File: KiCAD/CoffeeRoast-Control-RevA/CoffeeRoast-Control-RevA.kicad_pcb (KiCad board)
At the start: 2 copper layers, 160 x 100 mm, 68 parts, among them J1 24V_IN_FROM_230V_PSU_3A, J2 FAN_24V_PWM_3A, J3 SSR_INPUT_TO_EXTERNAL_SSR, J4 K_TYPE_THERMOCOUPLE, J5 USB_C_Receptacle_XKB_U262-16X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, Q1 IRLZ44N_OR_LOGIC_NMOS, Q2 2N7002_SSR_DRIVER, SW1 RESET_EN, SW2 BOOT, U1 ESP32-S3-WROOM-1, U2 MAX6675_SOIC8_3V3, U3 AMS1117-3.3, U4 24V_TO_5V_BUCK_MODULE_>=1A

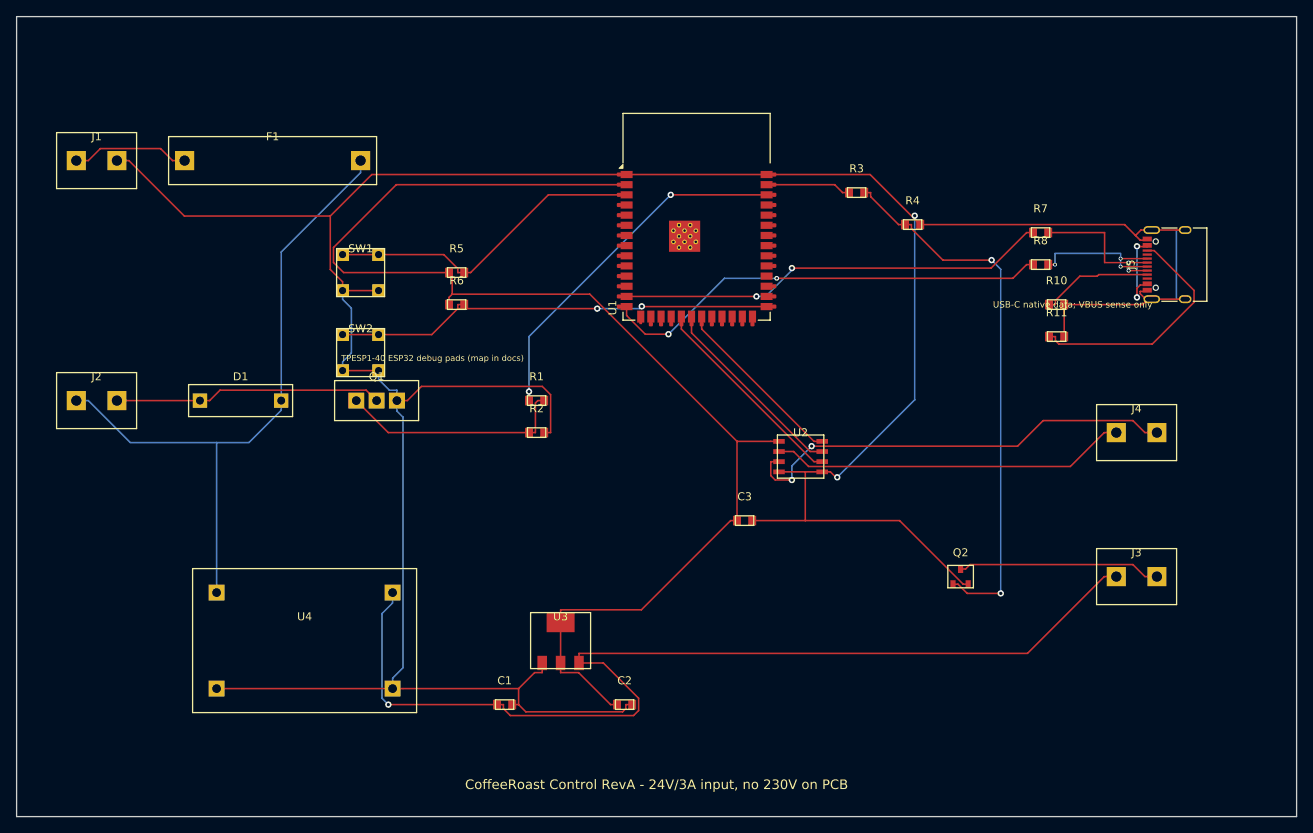
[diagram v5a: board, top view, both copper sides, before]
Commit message: Route labeled ESP32 solder pads outward
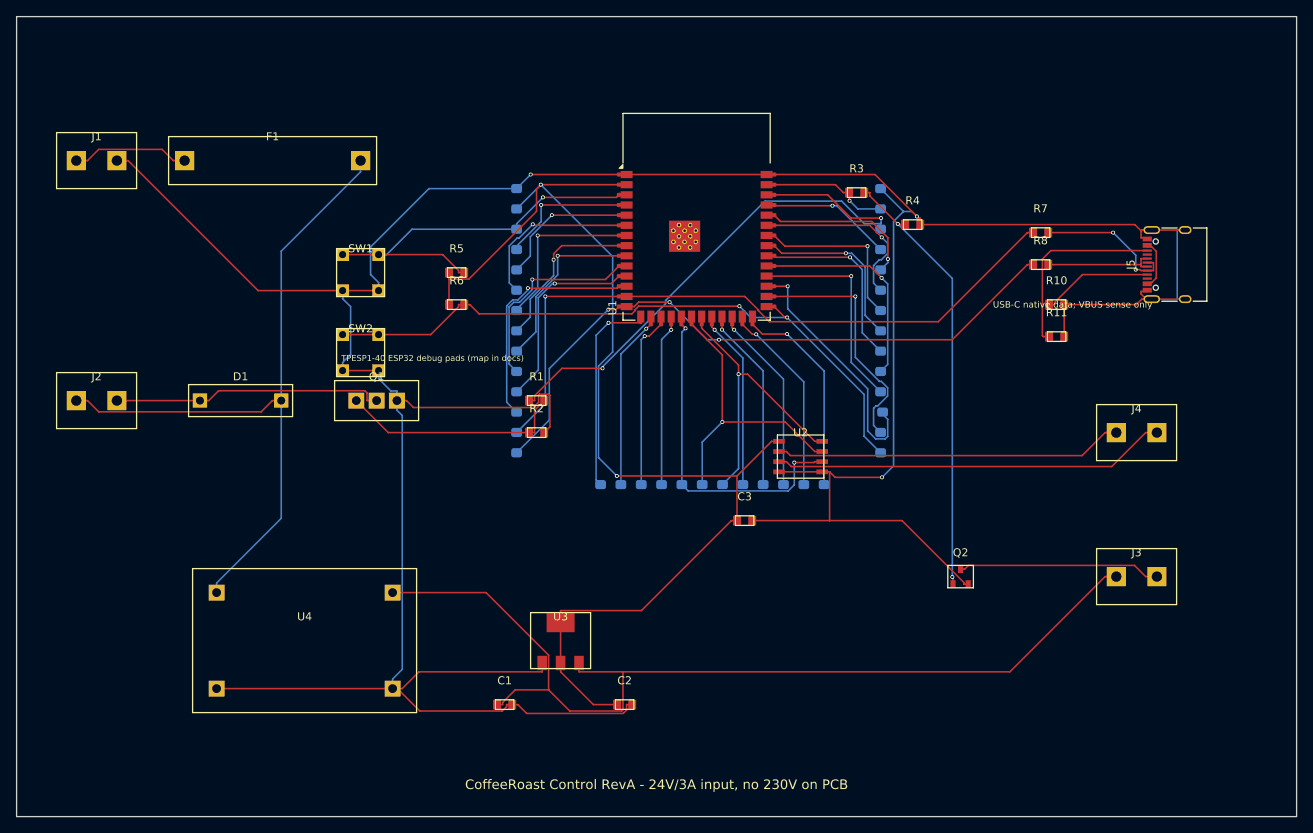
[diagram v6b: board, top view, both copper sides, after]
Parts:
- added PADESP1: GND, , B.Cu at (62.5, 21.5)
- added PADESP10: IO17, , B.Cu at (62.5, 44.4)
- added PADESP11: IO18, , B.Cu at (62.5, 46.9)
- added PADESP12: IO8, , B.Cu at (62.5, 49.4)
- added PADESP13: USB_D-, , B.Cu at (62.5, 52.0)
- added PADESP14: USB_D+, , B.Cu at (62.5, 54.5)
- added PADESP15: IO3, , B.Cu at (73.0, 58.5)
- added PADESP16: IO46, , B.Cu at (75.5, 58.5)
- added PADESP17: IO9, , B.Cu at (78.1, 58.5)
- added PADESP18: IO10, , B.Cu at (80.6, 58.5)
- added PADESP19: IO11, , B.Cu at (83.2, 58.5)
- added PADESP2: 3V3, , B.Cu at (62.5, 24.0)
- added PADESP20: IO12, , B.Cu at (85.7, 58.5)
- added PADESP21: IO13, , B.Cu at (88.2, 58.5)
- added PADESP22: IO14, , B.Cu at (90.8, 58.5)
- added PADESP23: IO21, , B.Cu at (93.3, 58.5)
- added PADESP24: IO47, , B.Cu at (95.9, 58.5)
- added PADESP25: IO48, , B.Cu at (98.4, 58.5)
- added PADESP26: IO45, , B.Cu at (100.9, 58.5)
- added PADESP27: IO0, , B.Cu at (108.0, 54.5)
- added PADESP28: IO35, , B.Cu at (108.0, 52.0)
- added PADESP29: IO36, , B.Cu at (108.2, 49.4)
- added PADESP3: EN, , B.Cu at (62.5, 26.6)
- added PADESP30: IO37, , B.Cu at (108.0, 46.9)
- added PADESP31: IO38, , B.Cu at (108.0, 44.4)
- added PADESP32: IO39, , B.Cu at (108.0, 41.8)
- added PADESP33: IO40, , B.Cu at (108.0, 39.3)
- added PADESP34: IO41, , B.Cu at (108.0, 36.7)
- added PADESP35: IO42, , B.Cu at (108.0, 34.2)
- added PADESP36: RXD0, , B.Cu at (108.0, 31.7)
- added PADESP37: TXD0, , B.Cu at (108.0, 29.1)
- added PADESP38: IO2, , B.Cu at (108.0, 26.6)
- added PADESP39: IO1, , B.Cu at (108.0, 24.0)
- added PADESP4: IO4, , B.Cu at (62.5, 29.1)
- added PADESP40: GND, , B.Cu at (108.0, 21.5)
- added PADESP5: IO5, , B.Cu at (62.5, 31.7)
- added PADESP6: IO6, , B.Cu at (62.5, 34.2)
- added PADESP7: IO7, , B.Cu at (62.5, 36.7)
- added PADESP8: IO15, , B.Cu at (62.5, 39.3)
- added PADESP9: IO16, , B.Cu at (62.5, 41.8)
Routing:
- net GPIO36: track 0.00 -> 31.3 mm, vias 0 -> 1
- net USB_DN_MCU: track 54.3 -> 85.4 mm, vias 2 -> 1
- net GPIO35: track 0.00 -> 31.1 mm, vias 0 -> 1
- net GPIO8: track 0.00 -> 29.9 mm, vias 0 -> 1
- net FAN_PWM: track 45.0 -> 73.1 mm
- net BOOT: track 55.8 -> 83.7 mm
- net GPIO38: track 0.00 -> 27.4 mm, vias 0 -> 1
- net GPIO37: track 0.00 -> 26.6 mm, vias 0 -> 1
- net GPIO45: track 0.00 -> 26.5 mm, vias 0 -> 1
- net GPIO17: track 0.00 -> 26.0 mm, vias 0 -> 1
- net GPIO3: track 0.00 -> 25.9 mm, vias 0 -> 1
- net USB_DP_MCU: track 56.5 -> 82.0 mm, vias 2 -> 3
- net GPIO18: track 0.00 -> 25.0 mm, vias 0 -> 1
- net GPIO48: track 0.00 -> 24.5 mm, vias 0 -> 1
- net GPIO39: track 0.00 -> 23.8 mm, vias 0 -> 1
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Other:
- board text added: "3V3"
- board text added: "EN"
- board text added: "ESP32 SOLDER PADS - BOTTOM"
- board text added: "GND"
- board text added: "IO0"
- board text added: "IO1"
- board text added: "IO10"
- board text added: "IO11"
- board text added: "IO12"
- board text added: "IO13"
- board text added: "IO14"
- board text added: "IO15"
- board text added: "IO16"
- board text added: "IO17"
- board text added: "IO18"
- board text added: "IO2"
- board text added: "IO21"
- board text added: "IO3"
- board text added: "IO35"
- board text added: "IO36"
- board text added: "IO37"
- board text added: "IO38"
- board text added: "IO39"
- board text added: "IO4"
- board text added: "IO40"
- board text added: "IO41"
- board text added: "IO42"
- board text added: "IO45"
- board text added: "IO46"
- board text added: "IO47"
- board text added: "IO48"
- board text added: "IO5"
- board text added: "IO6"
- board text added: "IO7"
- board text added: "IO8"
- board text added: "IO9"
- board text added: "RXD0"
- board text added: "TXD0"
- board text added: "USB_D+"
- board text added: "USB_D-"

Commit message: Improve CoffeeRoast RevA PCB robustness
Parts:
- added C4: 220uF_35V_INPUT_BULK, , F.Cu at (0.00, 0.00)
- added C5: 1nF_C0G_THERMO_DIFF_FILTER_DNP_IF_NOISY, , F.Cu at (0.00, 0.00)
- added D2: SMBJ33A_24V_INPUT_TVS, , F.Cu at (0.00, 0.00)
- added D3: SMBJ33A_FAN_TVS, , F.Cu at (0.00, 0.00)
- added TP24V: +24V_FUSED_TEST, , F.Cu at (0.00, 0.00)
- added TP3V3: +3V3_TEST, , F.Cu at (0.00, 0.00)
- added TP5V: +5V_TEST, , F.Cu at (0.00, 0.00)
- added TPGND: GND_TEST, , F.Cu at (0.00, 0.00)
- added U5: USBLC6-2SC6_OR_USB2_ESD, , F.Cu at (0.00, 0.00)
- Q1: value IRLZ44N_OR_LOGIC_NMOS -> IRLB8721_OR_3V3_LOGIC_NMOS_RDS_ON_LOW
- U3: value AMS1117-3.3 -> 3V3_SWITCHING_REGULATOR_>=600mA_5V_IN_REPLACES_AMS1117
- U4: value 24V_TO_5V_BUCK_MODULE_>=1A -> 24V_TO_5V_BUCK_MODULE_>=1A_LOW_NOISE
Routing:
- net GND: track 436.6 -> 447.8 mm
- net +24V_RAW: track 14.7 -> 22.9 mm
- net +24V_FUSED: track 88.2 -> 96.2 mm
- net THERMO_PLUS: track 43.6 -> 48.6 mm
- net THERMO_MINUS: track 49.3 -> 54.3 mm
- net FAN_NEG: track 34.1 -> 39.1 mm
- net +3V3: track 149.6 -> 153.6 mm
- net +5V: track 122.8 -> 125.8 mm

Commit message: feat: update RevA PCB and production artifacts
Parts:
- added C6: 100nF_U1_DECOUPLING_0603, , F.Cu at (73.2, 20.4)
- added C7: 100nF_U4_OUTPUT_DECOUPLING_0603, , F.Cu at (53.0, 72.7)
- added FID1: FIDUCIAL_GLOBAL_1MM, , F.Cu at (6.00, 6.00)
- added FID2: FIDUCIAL_GLOBAL_1MM, , F.Cu at (154.0, 6.00)
- added FID3: FIDUCIAL_GLOBAL_1MM, , F.Cu at (154.0, 94.0)
- added FID4: FIDUCIAL_GLOBAL_1MM, , B.Cu at (6.00, 6.00)
- added FID5: FIDUCIAL_GLOBAL_1MM, , B.Cu at (154.0, 6.00)
- added FID6: FIDUCIAL_GLOBAL_1MM, , B.Cu at (154.0, 94.0)
- added JGPIO1: ESP32_GPIO_BREAKOUT_ROW, ESP32_GPIO_BREAKOUT_ROW, F.Cu at (110.3, 92.0)
- added TPBOOT1: BOOT_TWEEZER_PADS, , F.Cu at (49.0, 42.0)
- added TPRESET1: RESET_TWEEZER_PADS, , F.Cu at (49.0, 32.0)
- added TPSSR1: SSR_OUT_MEAS_PADS, , F.Cu at (140.0, 76.2)
- moved C5 147.7 mm to (140.0, 47.0)
- moved U5 136.6 mm to (133.7, 28.0)
- moved TP3V3 104.7 mm to (72.0, 76.0)
- moved TPGND 97.8 mm to (50.0, 84.0)
- moved TP5V 87.7 mm to (50.0, 72.0)
- moved TP24V 75.3 mm to (22.0, 72.0)
- moved D3 44.1 mm to (10.0, 43.0)
- moved D2 28.0 mm to (10.0, 26.2)
- moved C4 25.3 mm to (10.0, 23.2)
- moved J5 9.00 mm to (154.0, 31.0)
- moved U1 3.00 mm to (85.0, 28.0)
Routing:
- net GPIO3: track 25.9 -> 71.5 mm
- net GPIO9: track 22.3 -> 68.0 mm
- net GPIO46: track 22.6 -> 68.2 mm
- net GPIO10: track 21.5 -> 67.1 mm
- net GPIO48: track 24.5 -> 61.5 mm
- net GPIO45: track 26.5 -> 63.5 mm
- net GND: track 447.8 -> 476.0 mm, vias 3 -> 5
- net +3V3: track 153.6 -> 171.7 mm, vias 2 -> 9
- net +5V: track 125.8 -> 138.0 mm
- net SSR_NEG: track 25.3 -> 37.3 mm
- net USB_DP: track 14.2 -> 23.2 mm
- net USB_CC2: track 24.0 -> 33.0 mm
- net USB_DN: track 18.0 -> 27.0 mm
- net USB_CC1: track 14.0 -> 23.0 mm
- net +24V_FUSED: track 96.2 -> 101.7 mm
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- added copper zone on B.Cu, net GND
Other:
- board text added: "+24V"
- board text added: "+5V"
- board text added: "+5V TP"
- board text added: "24V IN"
- board text added: "BOOT"
- board text added: "BOOT TP"
- board text added: "C1 10u"
- board text added: "C2 10u"
- board text added: "C3 100n"
- board text added: "C4 220uF"
- board text added: "C5 TC FILTER"
- board text added: "C6 100n U1"
- board text added: "C7 100n U4"
- board text added: "D1 FLYBACK"
- board text added: "D2 24V TVS"
- board text added: "D3 FAN TVS"
- board text added: "ESP32 GPIO BREAKOUT"
- board text added: "F1 FUSE"
- board text added: "FAN OUT"
- board text added: "FAN-"
- board text added: "GPIO0 BOOT"
- board text added: "GPIO1 SSR"
- board text added: "GPIO10"
- board text added: "GPIO11 DO"
- board text added: "GPIO12 CS"
- board text added: "GPIO13 CLK"
- board text added: "GPIO14"
- board text added: "GPIO15"
- board text added: "GPIO16"
- board text added: "GPIO17"
- board text added: "GPIO18"
- board text added: "GPIO19 D-"
- board text added: "GPIO2 FAN"
- board text added: "GPIO20 D+"
- board text added: "GPIO21"
- board text added: "GPIO3"
- board text added: "GPIO35"
- board text added: "GPIO36"
- board text added: "GPIO37"
- board text added: "GPIO38"
- board text added: "GPIO39"
- board text added: "GPIO4"
- board text added: "GPIO40"
- board text added: "GPIO41"
- board text added: "GPIO42"
- board text added: "GPIO45"
- board text added: "GPIO46"
- board text added: "GPIO47"
- board text added: "GPIO48"
- board text added: "GPIO5"
- board text added: "GPIO6"
- board text added: "GPIO7"
- board text added: "GPIO8"
- board text added: "GPIO9"
- board text added: "Q1 FAN MOSFET"
- board text added: "Q2 SSR DRV"
- board text added: "R1 100R"
- board text added: "R10 5k1"
- board text added: "R11 5k1"
- board text added: "R2 100k"
- board text added: "R3 100R"
- board text added: "R4 100k"
- board text added: "R5 10k"
- board text added: "R6 10k"
- board text added: "R7 27R"
- board text added: "R8 27R"
- board text added: "RESET"
- board text added: "RST"
- board text added: "RST TP"
- board text added: "RX0 GPIO44"
- board text added: "SSR MEAS"
- board text added: "SSR OUT"
- board text added: "SSR-"
- board text added: "SSR- TP"
- board text added: "TC+"
- board text added: "TC-"
- board text added: "THERMO"
- board text added: "TP24V"
- board text added: "TP3V3"
- board text added: "TP5V"
- board text added: "TPGND"
- board text added: "TX0 GPIO43"
- board text added: "U1 ESP32-S3"
- board text added: "U2 MAX6675"
- board text added: "U3 3V3 REG"
- board text added: "U4 24V->5V"
- board text added: "U5 USB ESD"
- board text added: "USB-C DATA"
- board text removed: "ESP32 SOLDER PADS - BOTTOM"
- board text removed: "IO0"
- board text removed: "IO1"
- board text removed: "IO10"
- board text removed: "IO11"
- board text removed: "IO12"
- board text removed: "IO13"
- board text removed: "IO14"
- board text removed: "IO15"
- board text removed: "IO16"
- board text removed: "IO17"
- board text removed: "IO18"
- board text removed: "IO2"
- board text removed: "IO21"
- board text removed: "IO3"
- board text removed: "IO35"
- board text removed: "IO36"
- board text removed: "IO37"
- board text removed: "IO38"
- board text removed: "IO39"
- board text removed: "IO4"
- board text removed: "IO40"
- board text removed: "IO41"
- board text removed: "IO42"
- board text removed: "IO45"
- board text removed: "IO46"
- board text removed: "IO47"
- board text removed: "IO48"
- board text removed: "IO5"
- board text removed: "IO6"
- board text removed: "IO7"
- board text removed: "IO8"
- board text removed: "IO9"
- board text removed: "RXD0"
- board text removed: "TXD0"
- board text removed: "USB_D+"
- board text removed: "USB_D-"
